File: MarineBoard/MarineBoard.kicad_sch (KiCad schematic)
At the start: 161 parts, among them CN1 MKDSN 1,5/ 2-5,08, CN2 MKDSN 1,5/ 2-5,08, CN3 SM04B-SRSS-TB (LF)(SN), CN4 BM10B-GHS-TBT, J1 USB_C_Receptacle_USB2.0_16P, Q2 S8050, Q3 S8050, Q4 BUK762R4-60E, U1 SY8089A1AAC, U11 SN65HVD230DR, U12 DB125-3.5-3P-GN-S, U13 DB125-3.5-3P-GN-S, U14 PC817C-S, U16 PC817C-S, U17 PC817C-S, U18 INA226, U19 INA226, U2 INA226, U21 PC817C-S, U22 SN74LVC1G14DBVR, U23 MCP1407-E/MF, U3 TPS5430DDA, U4 DB125-3.5-2P-GN-S, U5 DB125-3.5-2P-GN-S, U6 DB125-3.5-2P-GN-S, U7 DB125-3.5-3P-GN-S, U8 ESP32-S3-WROOM-2-N32R16V, U9 DB125-3.5-3P-GN-S

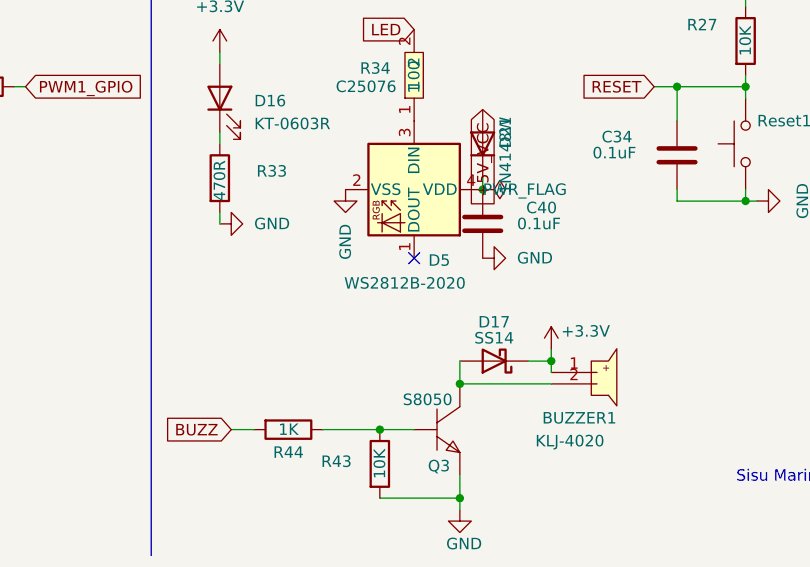
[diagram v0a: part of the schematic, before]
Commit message: Answer PCBWay's T-1P19 questions and fit the fuses and shunt
PCBWay inserts the MINI fuses into F1-F4 and fits the 1.27 mm shunt on JP1. F2 is Eaton ATM-1 because Littelfuse 0297001.WXNV is not a real part. Descriptions for D2/D3, D5, D21, R5/R6 and R47 match the replies.

#199
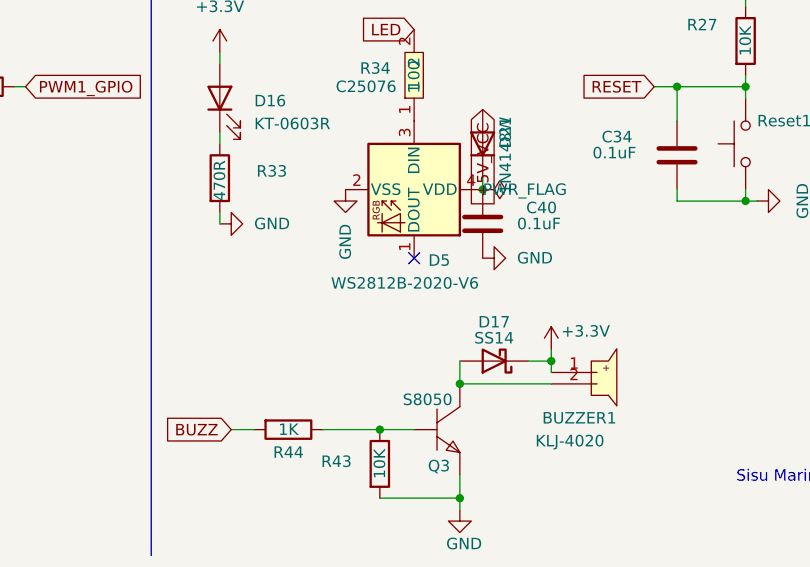
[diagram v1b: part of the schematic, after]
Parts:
- D5: value WS2812B-2020 -> WS2812B-2020-V6; MPN WS2812B-2020 -> WS2812B-2020-V6
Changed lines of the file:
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@@
 			)
 		)
-		(property "Description" "XF-506P MINI blade fuse holder"
+		(property "Description" "XF-506P MINI blade fuse holder. Insert Littelfuse 0297010.WXNV, 10 A 32 V MINI blade, into this holder."
 			(at 260.35 99.06 0)
 			(hide yes)
@@
 			)
 		)
-		(property "Description" "5V bidirectional ESD diode, DFN1006-2L (SOD-882 land)"
+		(property "Description" "5V bidirectional ESD diode H5VL10B. Manufacturer package DFN1006-2L. Board land is SOD-882, the same 1.0 x 0.6 mm pad."
 			(at 95.25 52.07 0)
 			(hide yes)
@@
 			)
 		)
-		(property "Description" "33 ohm +/-5% 0402"
+		(property "Description" "33 ohm +/-1% 0402"
 			(at 100.33 43.18 0)
 			(hide yes)
@@
 			)
 		)
-		(property "Value" "WS2812B-2020"
+		(property "Value" "WS2812B-2020-V6"
 			(at 326.644 258.064 90)
 			(show_name no)
@@
 			)
 		)
-		(property "Description" "RGB LED with integrated controller, 2.0 x 2.0 mm"
+		(property "Description" "RGB LED with integrated controller, Worldsemi WS2812B-2020-V6, 2.0 x 2.0 mm"
 			(at 327.66 247.65 0)
 			(hide yes)
@@
 			)
 		)
-		(property "MPN" "WS2812B-2020"
+		(property "MPN" "WS2812B-2020-V6"
 			(at 327.66 247.65 0)
 			(hide yes)
@@
 			)
 		)
-		(property "Description" "2.2 kohm +/-1% 1W 2512"
+		(property "Description" "2.2 kohm +/-1% 2W 2512"
 			(at 191.77 176.53 0)
 			(hide yes)
@@
 			)
 		)
-		(property "Description" "XF-506P MINI blade fuse holder"
+		(property "Description" "XF-506P MINI blade fuse holder. Insert Littelfuse 0297010.WXNV, 10 A 32 V MINI blade, into this holder."
 			(at 172.72 234.95 0)
 			(hide yes)
@@
 			)
 		)
-		(property "Description" "33 ohm +/-5% 0402"
+		(property "Description" "33 ohm +/-1% 0402"
 			(at 100.33 40.64 0)
 			(hide yes)
@@
 			)
 		)
-		(property "Description" "XF-506P MINI blade fuse holder"
+		(property "Description" "XF-506P MINI blade fuse holder. Insert Eaton Bussmann ATM-1, 1 A 32 V MINI blade, into this holder."
 			(at 205.74 76.2 0)
 			(hide yes)
@@
 			)
 		)
-		(property "Description" "1.27 mm 1x2 vertical pin header. Leave open; shunt is supplied loose."
+		(property "Description" "1.27 mm 1x2 vertical pin header. Fit BOOMELE shunt MPN 1.27, LCSC C150949, onto these pins."
 			(at 57.15 194.31 0)
 			(hide yes)
@@
 			)
 		)
-		(property "Description" "XF-506P MINI blade fuse holder"
+		(property "Description" "XF-506P MINI blade fuse holder. Insert Littelfuse 0297002.WXNV, 2 A 32 V MINI blade, into this holder."
 			(at 34.29 74.93 0)
 			(hide yes)
@@
 			)
 		)
-		(property "Description" "5V bidirectional ESD diode, DFN1006-2L (SOD-882 land)"
+		(property "Description" "5V bidirectional ESD diode H5VL10B. Manufacturer package DFN1006-2L. Board land is SOD-882, the same 1.0 x 0.6 mm pad."
 			(at 95.25 33.02 0)
 			(hide yes)
@@
 			)
 		)
-		(property "Description" "75V 150mA switching diode SOD-123; drops D5 VDD ~0.65 V so 3.3 V data meets WS2812B VIH (#183)"
+		(property "Description" "75V 150mA switching diode, SOD-123, Diodes Inc 1N4148W-7-F"
 			(at 335.28 242.57 0)
 			(hide yes)
